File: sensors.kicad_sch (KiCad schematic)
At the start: 15 parts, among them U2 MAX30102EFD+T, U3 MAX30208CLB+T, U4 BNO085, U5 BMP384

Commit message: Organized components in pcb layout editor
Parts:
- removed C10, C11, C9: 0.1 μF, Capacitor_SMD:C_0402_1005Metric, symbol Device:C
- removed R6: 10kΩ, Resistor_SMD:R_0402_1005Metric, symbol Device:R
- removed R7, R8: 4.7kΩ, Resistor_SMD:R_0402_1005Metric, symbol Device:R
- removed U4: BNO085, LGA-28_CEV, symbol I_Syst_inc:BNO085
- removed U5: BMP384, LGA10_2.0X2.0X0.95_BOS, symbol I_Syst_inc:BMP384
- added TP1: TestPoint, symbol Connector:TestPoint
- added U8: LSM6DSV80XTR, 1_I_Syst.inc:QFN_LSM6DSV80XTR_STM-M, symbol 1_I_Syst.inc:LSM6DSV80XTR
- U2: footprint 1_I-SYST_inc:21-1048_F143A5&plus_1_MXM-L -> 1_I_Syst.inc:21-1048_F143A5&plus_1_MXM-L
- U3: footprint 1_I-SYST_inc:21-100265_MXM -> 1_I_Syst.inc:21-100265_MXM
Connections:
- net GND: now also U8.1 (SDO/TA0), U8.6 (GND), U8.7 (GND)
- net P1.09: now also U8.14 (SDA)
- net P1.10: now also U8.13 (SCL)
- net P1.11  AIN4: now also U8.4 (INT1)
- net VDD: now also U8.12 (CS), U8.5 (VDDIO), U8.8 (VDD); no longer R3.1
- net at R3.2: now also U8.2 (SDx)
- net P2.06 renamed P2.03
- new net QVAR_SWIPE: R3.1, TP1.1
- no-connect marks 9 -> 10

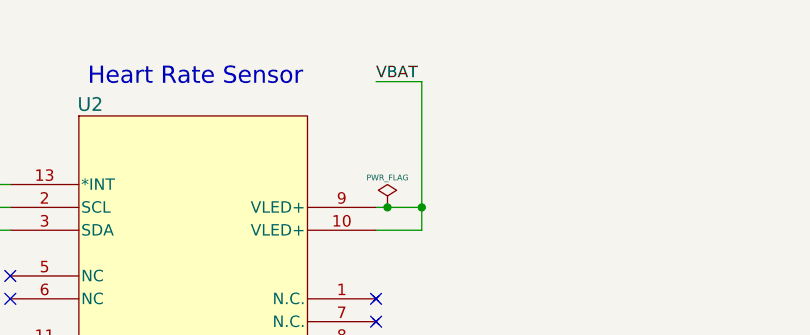
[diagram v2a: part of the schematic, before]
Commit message: PCB traces started
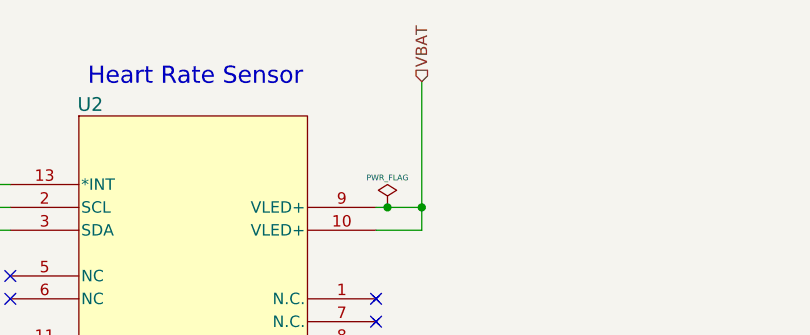
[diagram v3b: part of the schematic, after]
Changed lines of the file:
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@@
-	(wire
-		(pts
-			(xy 125.73 33.02) (xy 120.65 33.02)
-		)
-		(stroke
-			(width 0)
-			(type default)
-		)
-	)
 	(wire
 		(pts
@@
 		)
 	)
-	(label "VBAT"
-		(at 120.65 33.02 0)
-		(effects
-			(font
-				(size 1.27 1.27)
-			)
-			(justify left bottom)
-		)
-	)
 	(label "QVAR_SWIPE"
 		(at 171.45 91.44 0)
@@
 		)
 	)
+	(hierarchical_label "VBAT"
+		(shape input)
+		(at 125.73 33.02 90)
+		(effects
+			(font
+				(size 1.27 1.27)
+			)
+			(justify left)
+		)
+	)

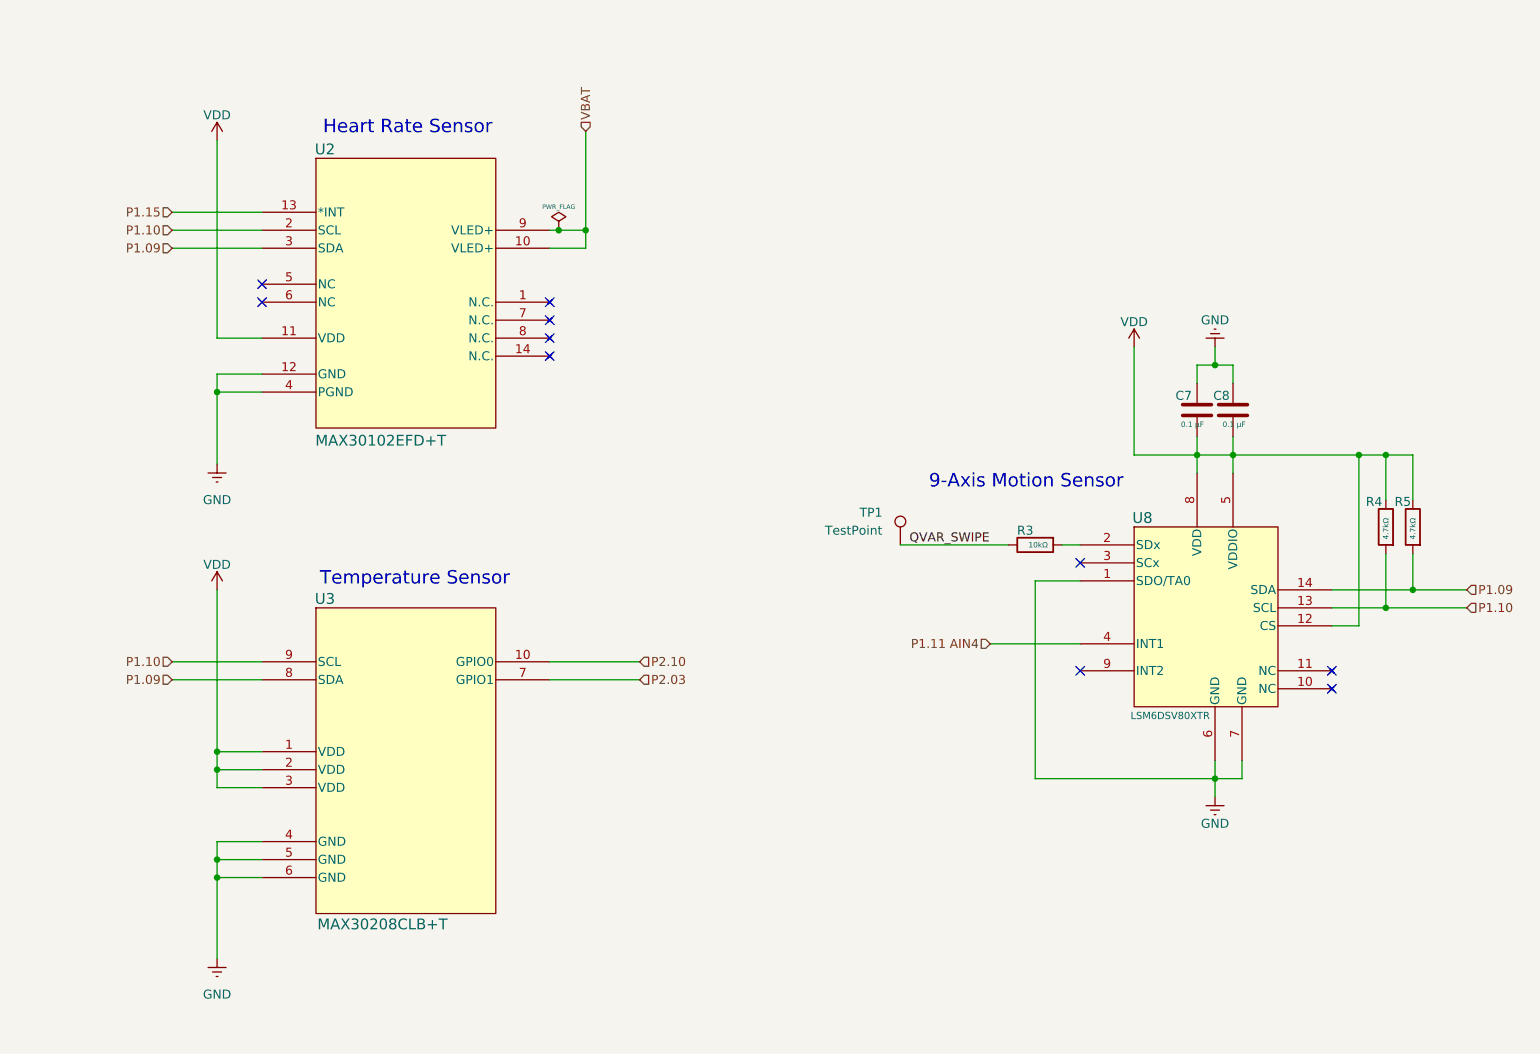
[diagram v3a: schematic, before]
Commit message: Full Redesign of the Watch PCB (DRC still not fully passed)
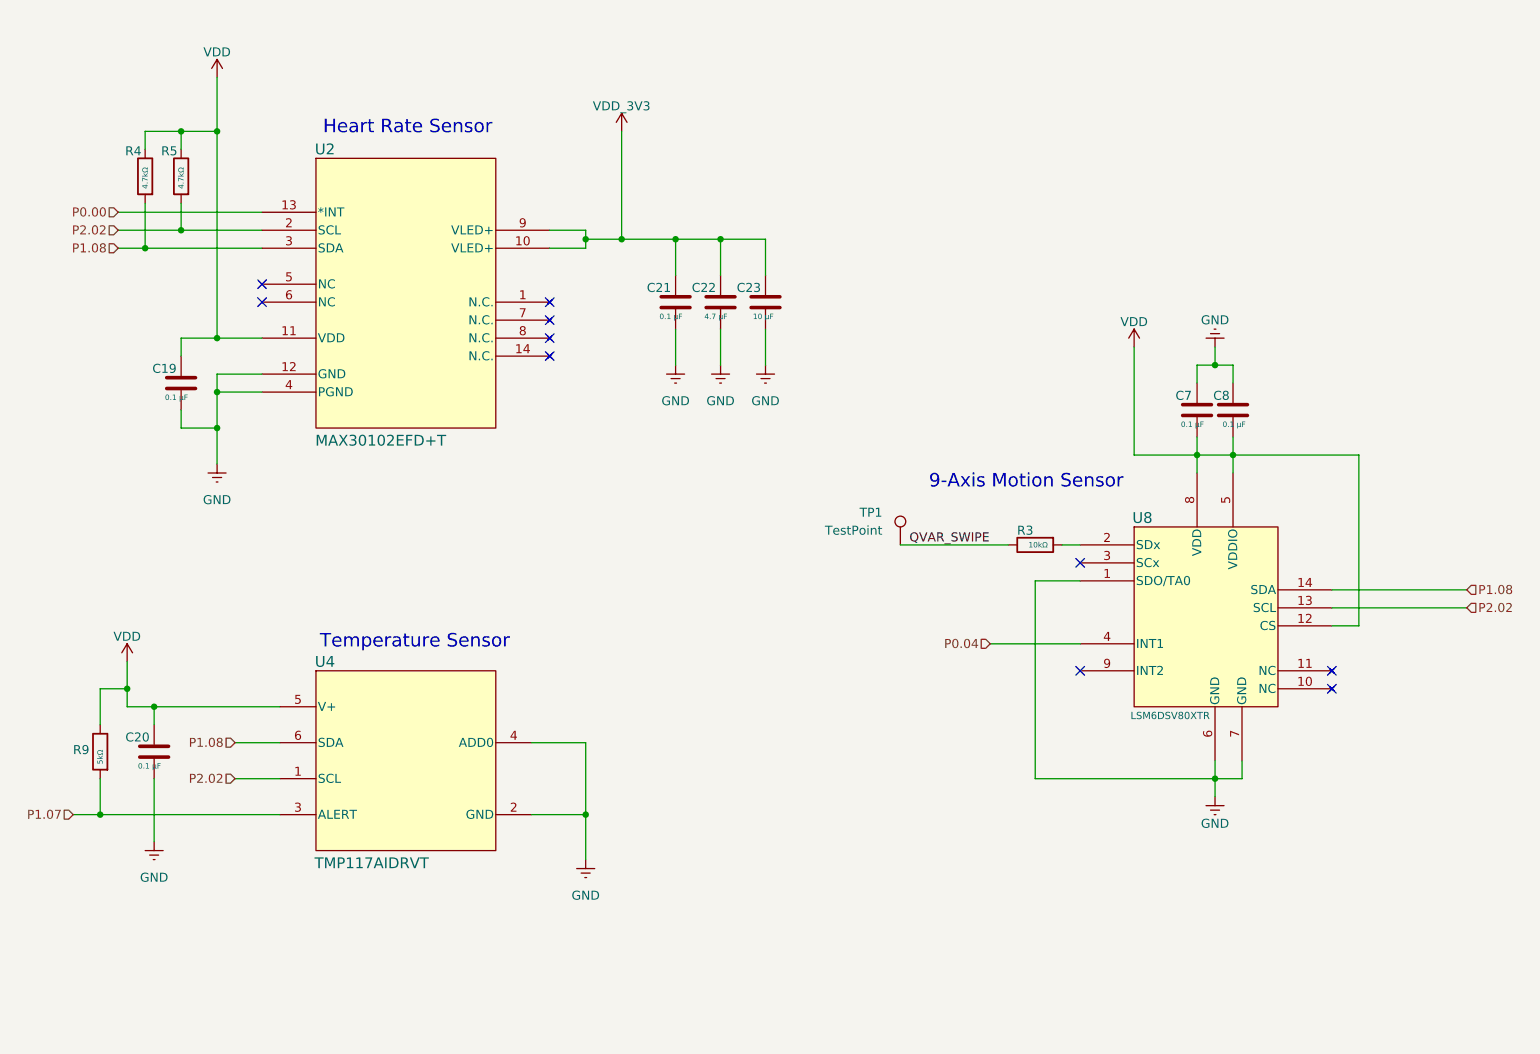
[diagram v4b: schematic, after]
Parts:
- removed U3: MAX30208CLB+T, 1_I_Syst.inc:21-100265_MXM, symbol I_Syst_inc:MAX30208CLB+T
- added C19, C20, C21: 0.1 μF, Capacitor_SMD:C_0402_1005Metric, symbol Device:C
- added C22: 4.7 μF, Capacitor_SMD:C_0402_1005Metric, symbol Device:C
- added C23: 10 μF, Capacitor_SMD:C_0402_1005Metric, symbol Device:C
- added R9: 5kΩ, Resistor_SMD:R_0402_1005Metric, symbol Device:R
- added U4: TMP117AIDRVT, 1_I_Syst.inc:DRV0006B, symbol 1_I_Syst.inc:TMP117AIDRVT
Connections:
- net GND: now also C19.2, C20.2, C21.2, C22.2, C23.2, U4.2 (GND), U4.4 (ADD0)
- net VDD: now also C19.1, C20.1, R9.1, U4.5 (V+)
- net P1.09 renamed P1.08
- net P1.08: now also R4.2, U4.6 (SDA); no longer R5.2
- net P1.10 renamed P2.02
- net P2.02: now also R5.2, U4.1 (SCL); no longer R4.2
- net P1.11  AIN4 renamed P0.04
- net P1.15 renamed P0.00
- net VBAT renamed VDD_3V3
- net VDD_3V3: now also C21.1, C22.1, C23.1
- new net P1.07: R9.2, U4.3 (ALERT)
